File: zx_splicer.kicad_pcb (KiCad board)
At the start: 2 copper layers, 45 x 90 mm, 8 parts, among them J1 Conn_02x04_Row_Letter_First, J2 Conn_02x23_Row_Letter_First, J3 Conn_02x04_Row_Letter_First, J4 Conn_02x23_Row_Letter_First, J5 Conn_02x04_Row_Letter_First, J6 Conn_02x23_Row_Letter_First, J7 Conn_02x04_Row_Letter_First, J8 Conn_02x23_Row_Letter_First

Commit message: Rename to ZX Splicer
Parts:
- J1: footprint zx_bus_breakout:short_board_socket -> zx_splicer:short_board_socket
- J2: footprint zx_bus_breakout:long_board_socket -> zx_splicer:long_board_socket
- J3: footprint zx_bus_breakout:short_pin_header -> zx_splicer:short_pin_header
- J4: footprint zx_bus_breakout:long_pin_header -> zx_splicer:long_pin_header
- J5: footprint zx_bus_breakout:short_pin_socket -> zx_splicer:short_pin_socket
- J6: footprint zx_bus_breakout:long_pin_socket -> zx_splicer:long_pin_socket
- J7: footprint zx_bus_breakout:short_board_edge -> zx_splicer:short_board_edge
- J8: footprint zx_bus_breakout:long_board_edge -> zx_splicer:long_board_edge
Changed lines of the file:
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@@
     (add_net /~WR)
   )
-  (module zx_bus_breakout:long_pin_socket (layer F.Cu)
+  (module zx_splicer:long_pin_socket (layer F.Cu)
     (at 78.74 63.5)
     (descr "Through hole straight socket strip, 2x23, 2.54mm pitch, double cols (from Kicad 4.0.7), script generated")
@@
     )
   )
-  (module zx_bus_breakout:long_pin_header (layer F.Cu)
+  (module zx_splicer:long_pin_header (layer F.Cu)
     (at 63.5 63.5)
     (descr "Through hole straight pin header, 2x23, 2.54mm pitch, double rows")
@@
     )
   )
-  (module zx_bus_breakout:short_pin_socket (layer F.Cu)
+  (module zx_splicer:short_pin_socket (layer F.Cu)
     (at 78.74 50.8)
     (descr "Through hole straight socket strip, 2x04, 2.54mm pitch, double cols (from Kicad 4.0.7), script generated")
@@
     )
   )
-  (module zx_bus_breakout:short_pin_header (layer F.Cu)
+  (module zx_splicer:short_pin_header (layer F.Cu)
     (at 63.5 50.8)
     (descr "Through hole straight pin header, 2x04, 2.54mm pitch, double rows")
@@
     )
   )
-  (module zx_bus_breakout:short_board_socket (layer F.Cu)
+  (module zx_splicer:short_board_socket (layer F.Cu)
     (at 51 50.8)
     (fp_text reference J1 (at 0 -2.54) (layer F.SilkS) hide
@@
       (net 8 /A15))
   )
-  (module zx_bus_breakout:long_board_socket (layer F.Cu)
+  (module zx_splicer:long_board_socket (layer F.Cu)
     (at 51 63.5)
     (fp_text reference J2 (at 0 -2.54) (layer F.SilkS) hide
@@
       (net 52 /D0))
   )
-  (module zx_bus_breakout:short_board_edge (layer F.Cu)
+  (module zx_splicer:short_board_edge (layer F.Cu)
     (at 96 50.8)
     (fp_text reference J7 (at 0 -2.54) (layer F.SilkS) hide
@@
       (net 8 /A15))
   )
-  (module zx_bus_breakout:long_board_edge (layer F.Cu)
+  (module zx_splicer:long_board_edge (layer F.Cu)
     (at 95.999999 63.5)
     (fp_text reference J8 (at 0 -2.54) (layer F.SilkS) hide

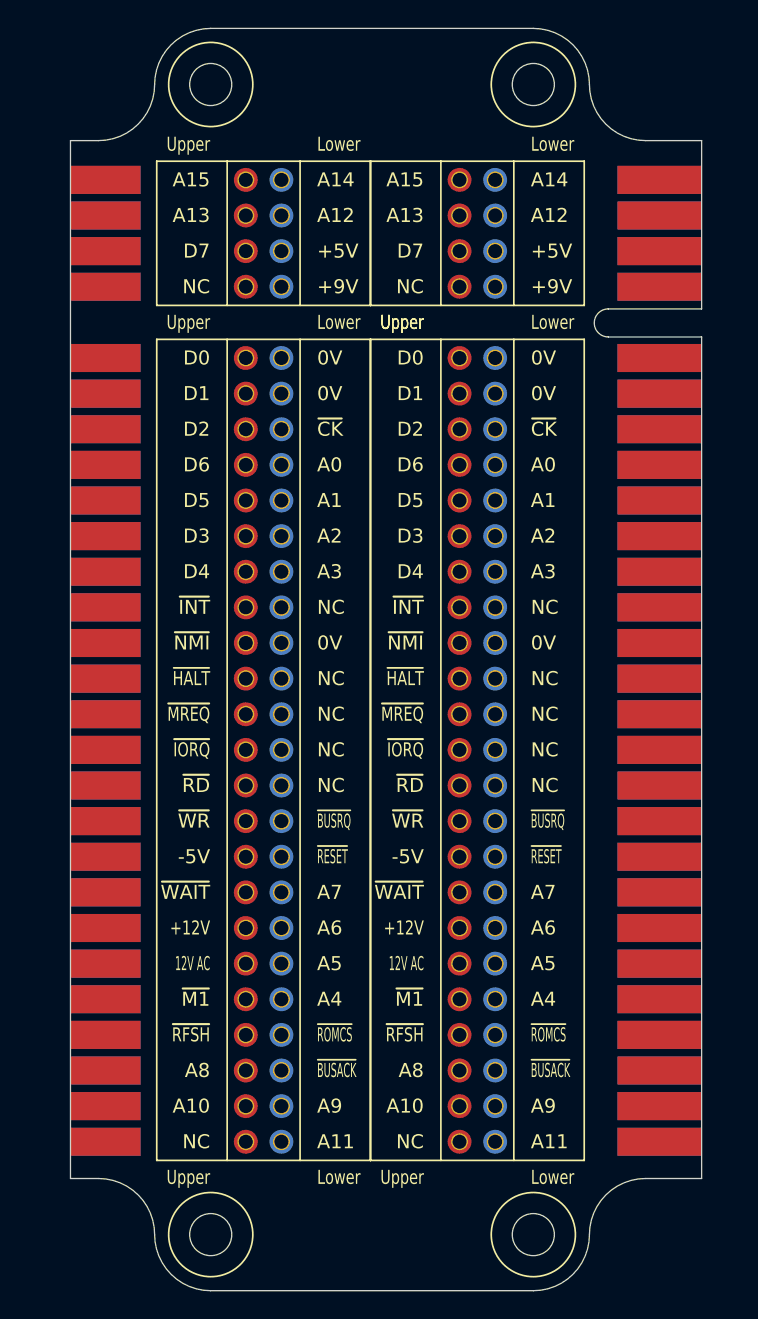
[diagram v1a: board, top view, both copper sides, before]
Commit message: PCB power and ground on inner layers
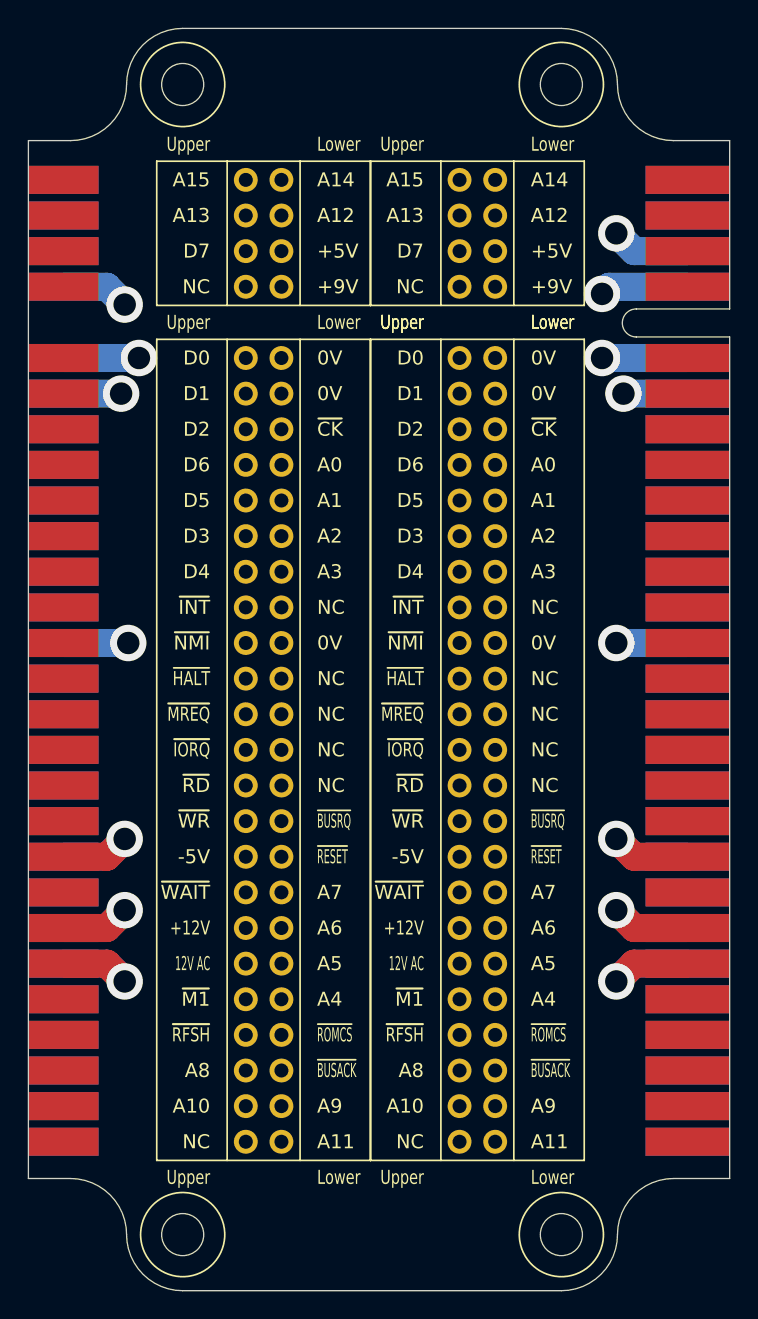
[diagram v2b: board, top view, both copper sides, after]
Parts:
- moved J7 1.00 mm to (95.0, 50.8)
- moved J8 1.00 mm to (95.0, 63.5)
- moved J1 0.50 mm to (50.5, 50.8)
- moved J2 0.50 mm to (50.5, 63.5)
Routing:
- net /0V: track 0.00 -> 29.9 mm, vias 0 -> 6
- net /+9V: track 0.00 -> 11.2 mm, vias 0 -> 2
- net /12V_AC: track 0.00 -> 10.5 mm, vias 0 -> 2
- net /-5V: track 0.00 -> 10.5 mm, vias 0 -> 2
- net /+12V: track 0.00 -> 10.5 mm, vias 0 -> 2
- net /+5V: track 0.00 -> 5.61 mm, vias 0 -> 1
- added copper zone on In1.Cu, net /+12V
- added copper zone on In1.Cu, net /+5V
- added copper zone on In1.Cu, net /+9V
- added copper zone on In1.Cu, net /-5V
- added copper zone on In2.Cu, net /0V
- added copper zone on In1.Cu, net /12V_AC
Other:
- board size 45 x 90 mm -> 50 x 90 mm
- copper layers 2 -> 4
- net class Default: trace_width 0.75 -> 0.25
- net class Ground added: clearance 0.2, trace_width 2, via_dia 2.6, via_drill 1.6
- net class Power added: clearance 0.2, trace_width 2, via_dia 2.6, via_drill 1.6

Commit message: Route all connections
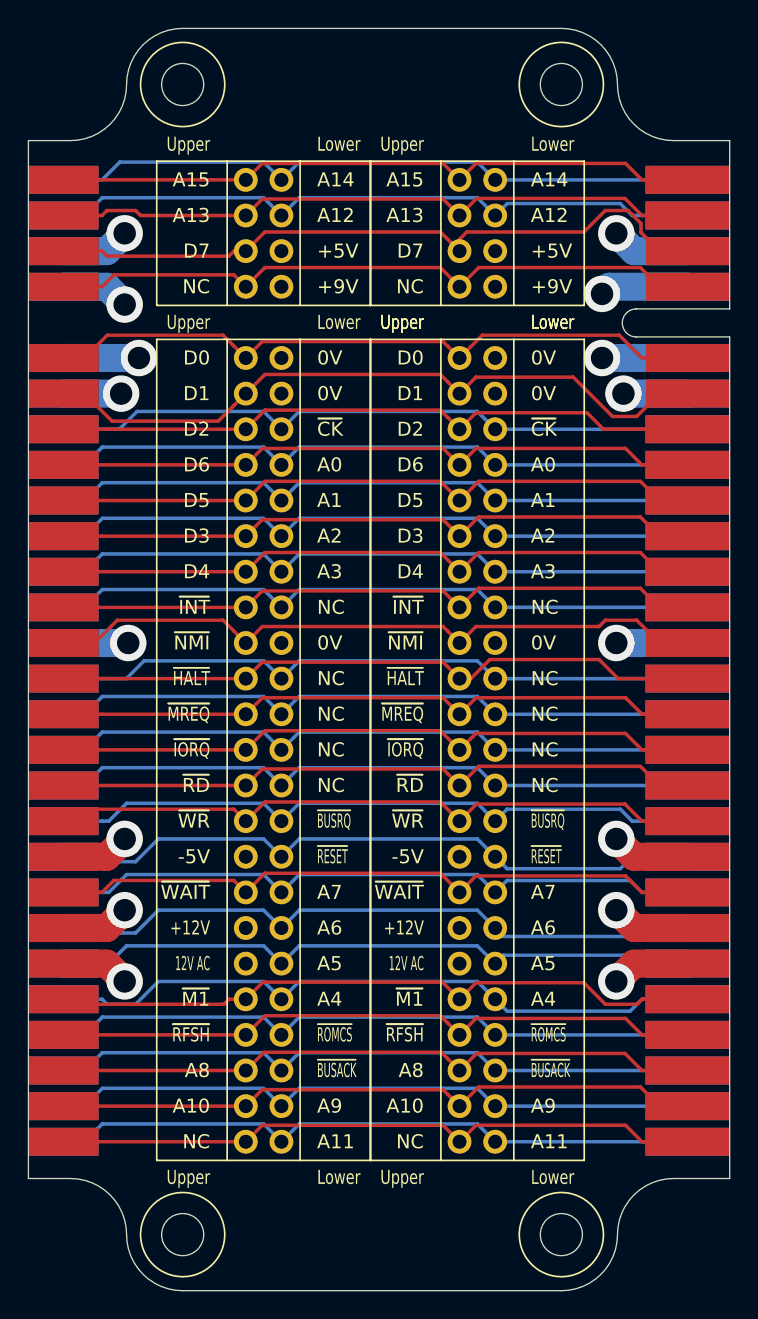
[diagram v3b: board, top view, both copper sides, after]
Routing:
- net /D1: track 0.00 -> 49.6 mm
- net /D7: track 0.00 -> 49.2 mm
- net /D0: track 0.00 -> 48.2 mm
- net /~NMI: track 0.00 -> 48.2 mm
- net /A4: track 0.00 -> 47.6 mm
- net /~RESET: track 0.00 -> 47.6 mm
- net /NC0: track 0.00 -> 47.5 mm
- net /A6: track 0.00 -> 47.4 mm
- net /~WR: track 0.00 -> 47.3 mm
- net /A12: track 0.00 -> 47.3 mm
- net /~BUSRQ: track 0.00 -> 47.3 mm
- net /A7: track 0.00 -> 47.3 mm
- net /~WAIT: track 0.00 -> 47.3 mm
- net /A5: track 0.00 -> 47.1 mm
- net /~M1: track 0.00 -> 47.1 mm
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
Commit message: Remove JLCPCB silkscreen text placeholder
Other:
- board text removed: "JLCJLCJLCJLC"
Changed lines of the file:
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@@
   (general
     (thickness 1.6)
-    (drawings 34)
+    (drawings 33)
     (tracks 518)
     (zones 0)
@@
   (layers
     (0 F.Cu signal)
-    (1 In1.Cu power hide)
-    (2 In2.Cu power hide)
+    (1 In1.Cu power)
+    (2 In2.Cu power)
     (31 B.Cu signal)
-    (32 B.Adhes user hide)
-    (33 F.Adhes user hide)
-    (34 B.Paste user hide)
-    (35 F.Paste user hide)
-    (36 B.SilkS user hide)
+    (32 B.Adhes user)
+    (33 F.Adhes user)
+    (34 B.Paste user)
+    (35 F.Paste user)
+    (36 B.SilkS user)
     (37 F.SilkS user)
-    (38 B.Mask user hide)
-    (39 F.Mask user hide)
-    (40 Dwgs.User user hide)
-    (41 Cmts.User user hide)
-    (42 Eco1.User user hide)
-    (43 Eco2.User user hide)
+    (38 B.Mask user)
+    (39 F.Mask user)
+    (40 Dwgs.User user)
+    (41 Cmts.User user)
+    (42 Eco1.User user)
+    (43 Eco2.User user)
     (44 Edge.Cuts user)
-    (45 Margin user hide)
-    (46 B.CrtYd user hide)
-    (47 F.CrtYd user hide)
-    (48 B.Fab user hide)
-    (49 F.Fab user hide)
+    (45 Margin user)
+    (46 B.CrtYd user)
+    (47 F.CrtYd user)
+    (48 B.Fab user)
+    (49 F.Fab user)
   )
   (setup
@@
     )
   )
-  (gr_text JLCJLCJLCJLC (at 86.079999 85 90) (layer B.SilkS)
-    (effects (font (size 1 1) (thickness 0.15)) (justify mirror))
-  )
   (gr_text "ZX Splicer 128K\nv1 by spbnick" (at 72.255 85 90) (layer B.SilkS)
